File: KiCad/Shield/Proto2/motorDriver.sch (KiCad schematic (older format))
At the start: 8 parts, among them J2 CONN_01X04, U2 L298_TH

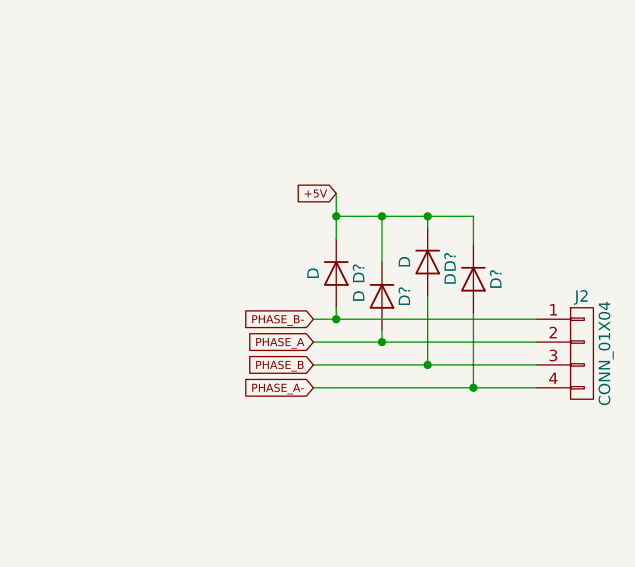
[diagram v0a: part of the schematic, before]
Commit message: added pngs of pcbs
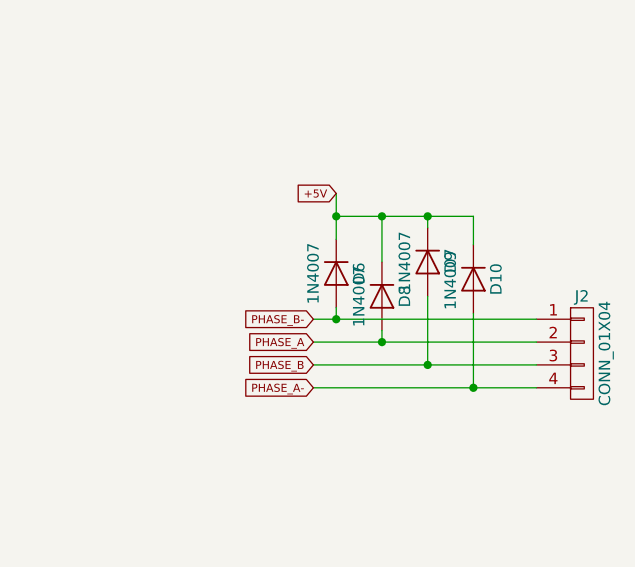
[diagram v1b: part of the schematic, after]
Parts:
- D10, D6, D8, D9: renamed from D?; value D -> 1N4007
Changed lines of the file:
@@
 MOTOR_VSS
 $Comp
-L D D?
+L D D6
 U 1 1 5AD30C7C
 P 7725 2550
-F 0 "D?" H 7725 2650 50  0000 C CNN
-F 1 "D" H 7725 2450 50  0000 C CNN
+F 0 "D6" H 7725 2650 50  0000 C CNN
+F 1 "1N4007" H 7725 2450 50  0000 C CNN
 F 2 "Diodes_THT:D_T-1_P10.16mm_Horizontal" H 7725 2550 50  0001 C CNN
 F 3 "" H 7725 2550 50  0001 C CNN
@@
 $EndComp
 $Comp
-L D D?
+L D D8
 U 1 1 5AD30CDD
 P 7925 2650
-F 0 "D?" H 7925 2750 50  0000 C CNN
-F 1 "D" H 7925 2550 50  0000 C CNN
+F 0 "D8" H 7925 2750 50  0000 C CNN
+F 1 "1N4007" H 7925 2550 50  0000 C CNN
 F 2 "Diodes_THT:D_T-1_P10.16mm_Horizontal" H 7925 2650 50  0001 C CNN
 F 3 "" H 7925 2650 50  0001 C CNN
@@
 $EndComp
 $Comp
-L D D?
+L D D9
 U 1 1 5AD30D5B
 P 8125 2500
-F 0 "D?" H 8125 2600 50  0000 C CNN
-F 1 "D" H 8125 2400 50  0000 C CNN
+F 0 "D9" H 8125 2600 50  0000 C CNN
+F 1 "1N4007" H 8125 2400 50  0000 C CNN
 F 2 "Diodes_THT:D_T-1_P10.16mm_Horizontal" H 8125 2500 50  0001 C CNN
 F 3 "" H 8125 2500 50  0001 C CNN
@@
 $EndComp
 $Comp
-L D D?
+L D D10
 U 1 1 5AD30D96
 P 8325 2575
-F 0 "D?" H 8325 2675 50  0000 C CNN
-F 1 "D" H 8325 2475 50  0000 C CNN
+F 0 "D10" H 8325 2675 50  0000 C CNN
+F 1 "1N4007" H 8325 2475 50  0000 C CNN
 F 2 "Diodes_THT:D_T-1_P10.16mm_Horizontal" H 8325 2575 50  0001 C CNN
 F 3 "" H 8325 2575 50  0001 C CNN
@@
 Connection ~ 1675 875
 Connection ~ 5850 3600
-Wire Wire Line
-	7925 2850 7925 2800
-Wire Wire Line
-	8125 2650 8125 2950
-Wire Wire Line
-	8325 2725 8325 3050
 Connection ~ 8325 3050
 Connection ~ 8125 2950
@@
 	7725 2300 8325 2300
 Connection ~ 7925 2300
-Wire Wire Line
-	7725 2700 7725 2750
 Wire Wire Line
 	7625 2750 8600 2750
@@
 Text GLabel 7725 2200 0    35   Input ~ 0
 +5V
+Wire Wire Line
+	7725 2700 7725 2750
+Wire Wire Line
+	7925 2800 7925 2850
+Wire Wire Line
+	8125 2650 8125 2950
+Wire Wire Line
+	8325 2725 8325 3050
 $EndSCHEMATC
